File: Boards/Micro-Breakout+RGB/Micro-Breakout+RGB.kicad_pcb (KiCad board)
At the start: 2 copper layers, 92.7 x 54.6 mm, 37 parts, among them J1 Conn_01x04, J10 Conn_01x17, J11 Conn_01x04, J12 Conn_01x04, J13 Conn_01x02, J14 Conn_01x04, J16 Conn_01x04, J17 Conn_01x04, J18 Conn_01x04, J2 Conn_01x04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

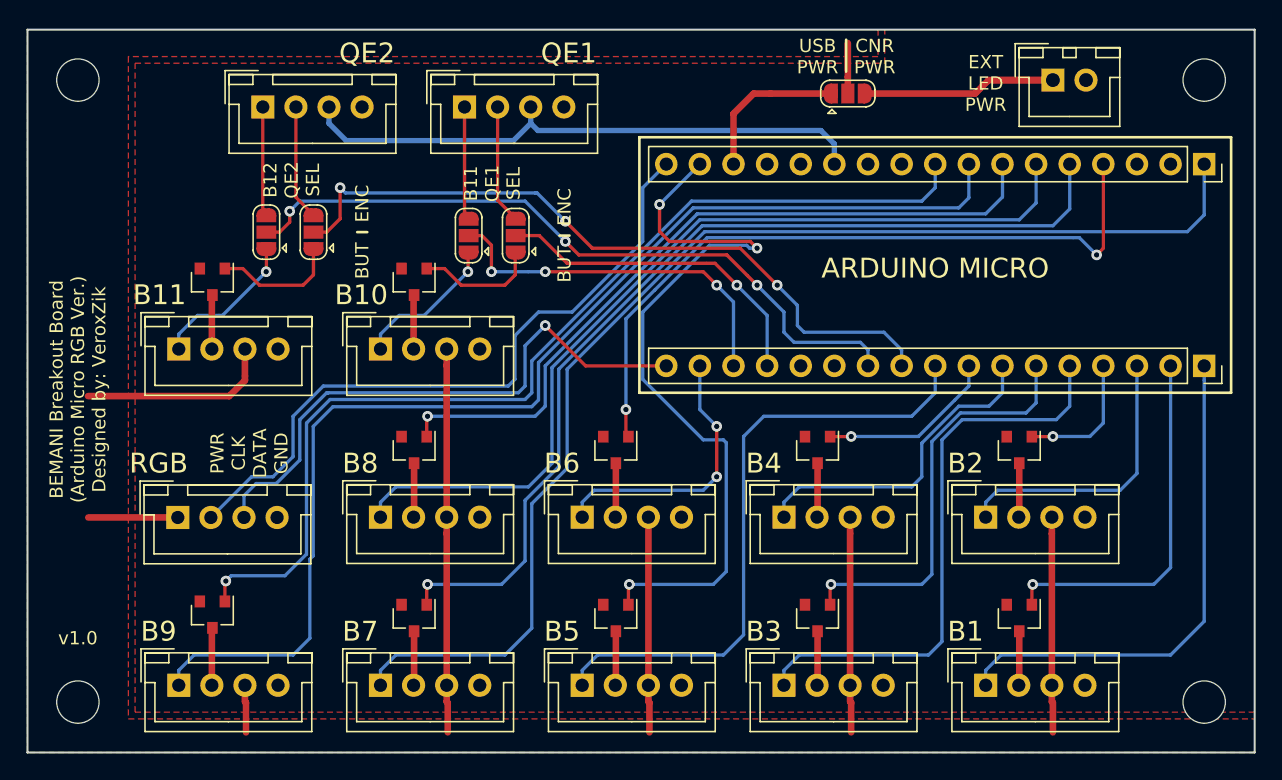
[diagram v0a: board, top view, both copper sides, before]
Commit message: Update both micro boards to v1.1
Fixes 5V on the LED connector
Adds pinout labels for Encoder / Button connectors
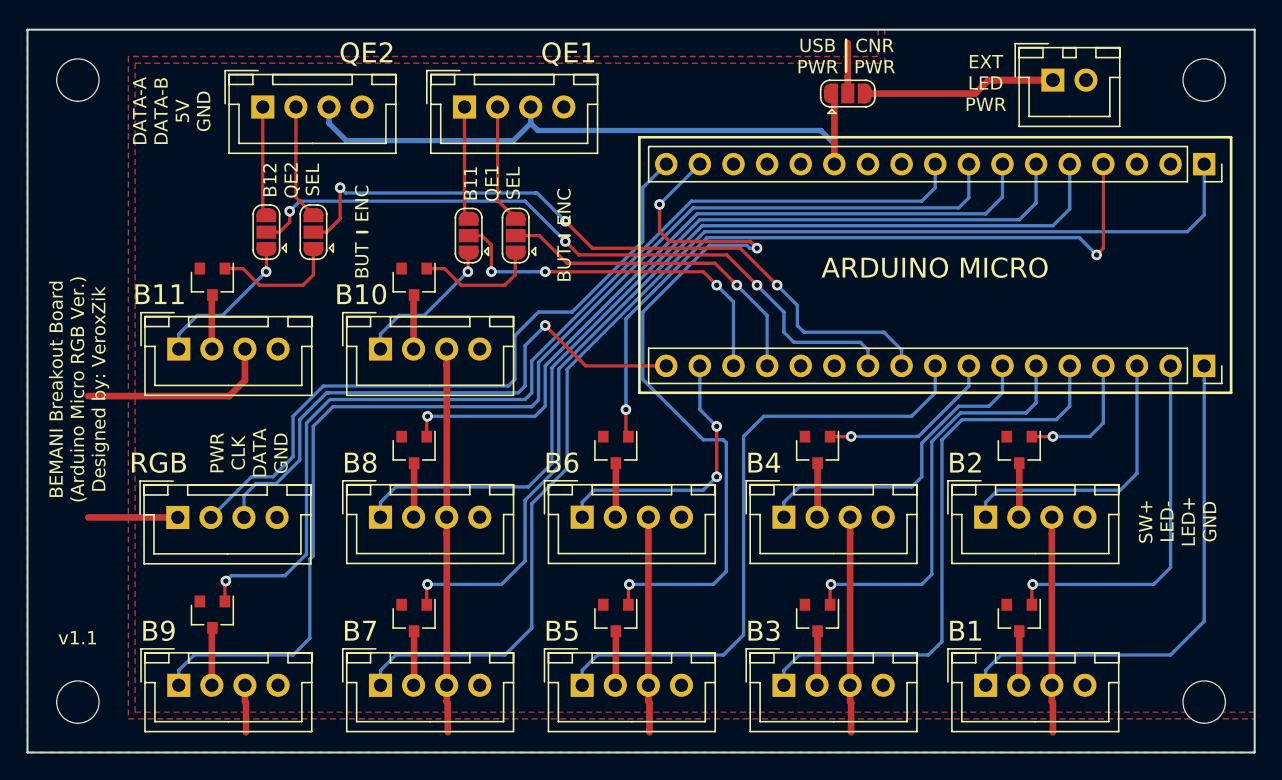
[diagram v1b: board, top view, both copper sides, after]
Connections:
- J7 pad 15: VBUS -> Net-(J7-Pad15)
- JP1 pad 1: VBUS -> +5V
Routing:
- net VBUS: track 11.8 -> 0.00 mm
- net +5V: track 43.9 -> 49.4 mm
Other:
- board text added: "DATA-A DATA-B 5V GND"
- board text added: "SW+ LED- LED+ GND"
- board text added: "v1.1"
- board text removed: "v1.0"

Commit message: Update Micro-RGB to v1.2
This shifts the SS and MISO pins to B9 in an attempt to consolidate potentially nonfunctional pins while using the SPI port for RGB functionality.
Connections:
- J10 pad 16: /B6 -> /B9LED
- J7 pad 16: /B5LED -> /B9
- J7 pad 8: /B9 -> /B6
- J7 pad 9: /B9LED -> /B5LED
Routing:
- net /B6: track 21.0 -> 52.9 mm, vias 2 -> 1
- net /B9LED: track 76.5 -> 48.9 mm, vias 1 -> 2
- net /B9: track 89.0 -> 68.2 mm
- net /B5LED: track 57.5 -> 62.0 mm, vias 3 -> 2
- net /B6LED: track 54.7 -> 57.9 mm
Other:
- board text added: "v1.2"
- board text removed: "v1.1"

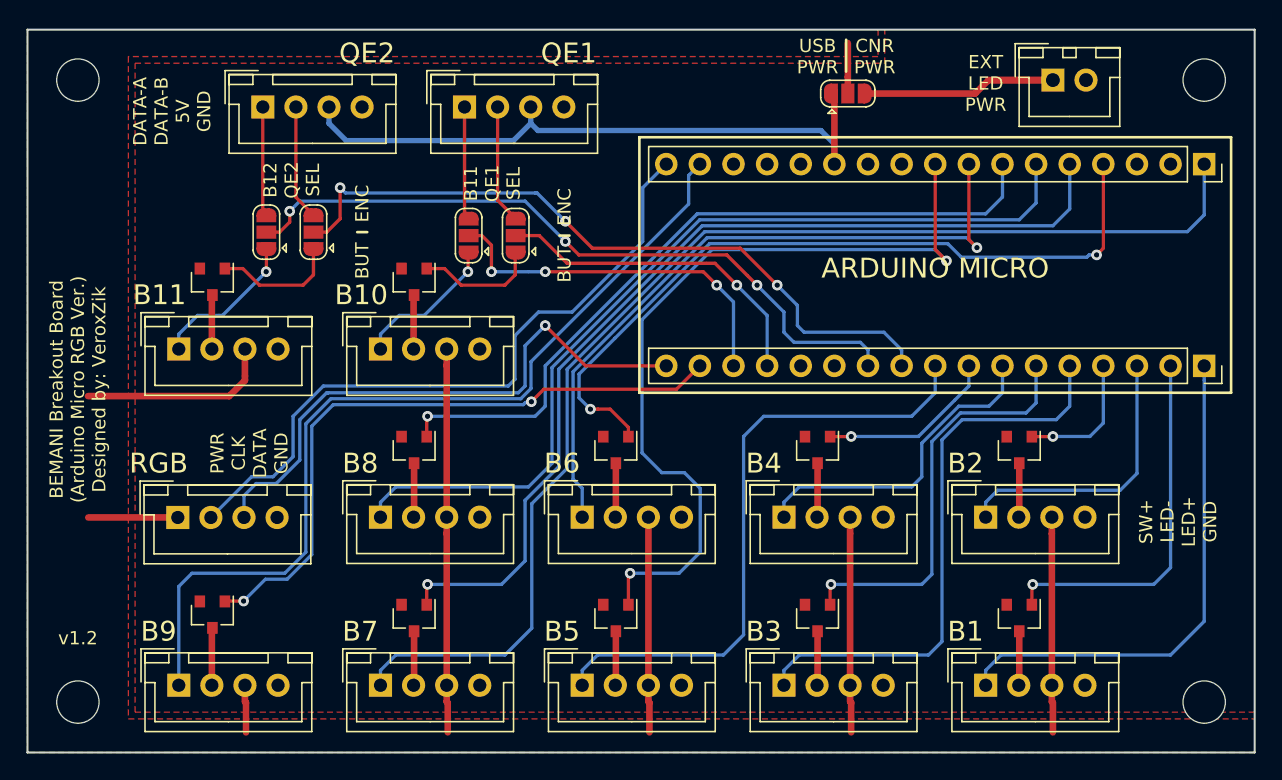
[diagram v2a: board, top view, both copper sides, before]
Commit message: Update MicroBreakout+RGB board.
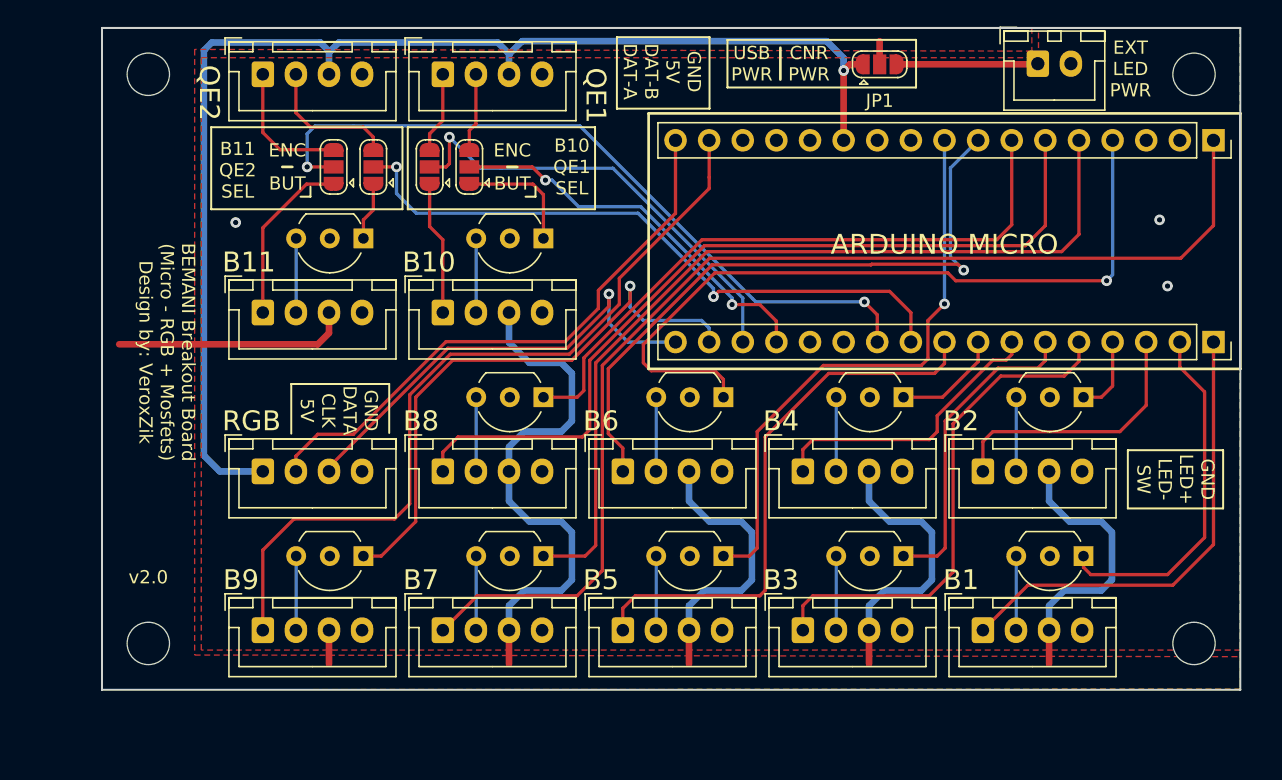
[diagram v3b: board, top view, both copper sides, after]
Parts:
- J1, J11, J12, J14, J16, J17, J18, J2, J3, J4, J5, J6, J8, J9: footprint Connectors_JST:JST_XH_B04B-XH-A_04x2.50mm_Straight -> Connector_JST:JST_XH_B4B-XH-A_1x04_P2.50mm_Vertical
- J13: footprint Connectors_JST:JST_XH_B02B-XH-A_02x2.50mm_Straight -> Connector_JST:JST_XH_B2B-XH-A_1x02_P2.50mm_Vertical
- Q1, Q10, Q11, Q12, Q2, Q3, Q4, Q5, Q6, Q7, Q8: value Si2302CDS -> 2N7000; footprint TO_SOT_Packages_SMD:SOT-23 -> Package_TO_SOT_THT:TO-92_Inline_Wide
- moved Q12 12.2 mm to (128.2, 127.4), turned to 180 degrees
- moved Q11 11.9 mm to (128.2, 103.4), turned to 180 degrees
- moved Q7 10.8 mm to (141.8, 127.4), turned to 180 degrees
- moved Q10 10.5 mm to (141.8, 115.4), turned to 180 degrees
- moved Q8 10.3 mm to (141.8, 103.4), turned to 180 degrees
- moved Q5 9.38 mm to (155.4, 127.4), turned to 180 degrees
- moved Q6 9.05 mm to (155.4, 115.4), turned to 180 degrees
- moved Q3 8.00 mm to (169.1, 127.4), turned to 180 degrees
- moved Q4 7.61 mm to (169.1, 115.4), turned to 180 degrees
- moved J18 7.59 mm to (120.7, 133.0)
- moved J14 7.31 mm to (120.7, 121.0)
- moved JP4 7.08 mm to (126.0, 98.0)
- moved J17 6.92 mm to (120.7, 109.0)
- moved MH1 6.92 mm to (112.0, 134.0)
- moved Q1 6.74 mm to (182.7, 127.4), turned to 180 degrees
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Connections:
- J10 pad 13: Net-(J10-Pad13) -> unconnected-(J10-Pad13)
- J14 pad 1: /LED+ -> +5V
- J7 pad 10: Net-(J7-Pad10) -> unconnected-(J7-Pad10)
- J7 pad 11: Net-(J7-Pad11) -> unconnected-(J7-Pad11)
- J7 pad 13: Net-(J7-Pad13) -> unconnected-(J7-Pad13)
- J7 pad 15: Net-(J7-Pad15) -> unconnected-(J7-Pad15)
- J7 pad 3: Net-(J7-Pad3) -> unconnected-(J7-Pad3)
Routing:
- net +5V: track 49.4 -> 97.2 mm, vias 0 -> 1
- net /LED+: track 107.1 -> 127.2 mm
- net /B5LED: track 62.0 -> 43.8 mm, vias 2 -> 1
- net /LDAT: track 43.8 -> 35.3 mm
- net +12V: track 19.2 -> 10.7 mm
- net /LCLK: track 51.6 -> 43.7 mm
- net /B3LED: track 31.4 -> 23.9 mm, vias 1 -> 0
- net /B8LED: track 56.1 -> 48.6 mm, vias 1 -> 0
- net /B9: track 68.2 -> 60.7 mm
- net /B7LED: track 72.2 -> 65.7 mm, vias 1 -> 0
- net /PIN1: track 28.1 -> 34.1 mm, vias 3 -> 1
- net /B4LED: track 13.6 -> 8.23 mm, vias 1 -> 0
- net /B5: track 47.3 -> 42.0 mm
- net /PIN3: track 54.4 -> 49.2 mm, vias 3 -> 2
- net /B11LED: track 9.46 -> 4.41 mm
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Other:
- board size 92.7 x 54.6 mm -> 86 x 50 mm
- net class Default removed
- rule pad_to_mask_clearance: 0.2 -> 0
- board text added: "B10 QE1 SEL"
- board text added: "B11 QE2 SEL"
- board text added: "BEMANI Breakout Board (Micro - RGB + Mosfets) Design by: VeroxZik"
- board text added: "GND 5V DAT-B DAT-A"
- board text added: "GND DATA CLK 5V"
- board text added: "GND LED+ LED- SW"
- board text added: "v2.0"
- board text removed: "B11 QE1 SEL"
- board text removed: "B12 QE2 SEL"
- board text removed: "BEMANI Breakout Board (Arduino Micro RGB Ver.) Designed by: VeroxZik"
- board text removed: "DATA-A DATA-B 5V GND"
- board text removed: "PWR CLK DATA GND"
- board text removed: "SW+ LED- LED+ GND"
- board text removed: "v1.2"
